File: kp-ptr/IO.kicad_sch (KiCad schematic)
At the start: 0 parts

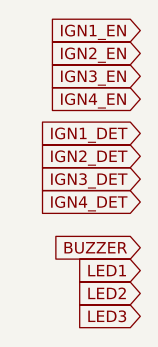
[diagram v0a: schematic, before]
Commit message: IGN & PSU added
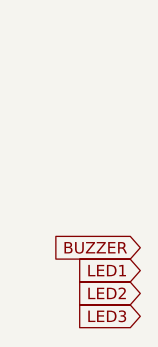
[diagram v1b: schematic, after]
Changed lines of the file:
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@@
 (kicad_sch (version 20211123) (generator eeschema)
   (paper "A4")
-  (global_label "IGN3_DET" (shape input) (at 36.83 41.91 180) (fields_autoplaced)
-    (effects (font (size 1.27 1.27)) (justify right))
-    (property "Intersheet References" "${INTERSHEET_REFS}" (id 0) (at 25.6479 41.8306 0)
-      (effects (font (size 1.27 1.27)) (justify right) hide)
-    )
-  )
-  (global_label "IGN1_EN" (shape input) (at 36.83 25.4 180) (fields_autoplaced)
-    (effects (font (size 1.27 1.27)) (justify right))
-    (property "Intersheet References" "${INTERSHEET_REFS}" (id 0) (at 26.555 25.3206 0)
-      (effects (font (size 1.27 1.27)) (justify right) hide)
-    )
-  )
   (global_label "LED3" (shape input) (at 36.83 57.15 180) (fields_autoplaced)
     (effects (font (size 1.27 1.27)) (justify right))
@@
     (effects (font (size 1.27 1.27)) (justify right))
     (property "Intersheet References" "${INTERSHEET_REFS}" (id 0) (at 29.7602 51.9906 0)
-      (effects (font (size 1.27 1.27)) (justify right) hide)
-    )
-  )
-  (global_label "IGN1_DET" (shape input) (at 36.83 36.83 180) (fields_autoplaced)
-    (effects (font (size 1.27 1.27)) (justify right))
-    (property "Intersheet References" "${INTERSHEET_REFS}" (id 0) (at 25.6479 36.7506 0)
-      (effects (font (size 1.27 1.27)) (justify right) hide)
-    )
-  )
-  (global_label "IGN3_EN" (shape input) (at 36.83 30.48 180) (fields_autoplaced)
-    (effects (font (size 1.27 1.27)) (justify right))
-    (property "Intersheet References" "${INTERSHEET_REFS}" (id 0) (at 26.555 30.4006 0)
-      (effects (font (size 1.27 1.27)) (justify right) hide)
-    )
-  )
-  (global_label "IGN2_DET" (shape input) (at 36.83 39.37 180) (fields_autoplaced)
-    (effects (font (size 1.27 1.27)) (justify right))
-    (property "Intersheet References" "${INTERSHEET_REFS}" (id 0) (at 25.6479 39.2906 0)
       (effects (font (size 1.27 1.27)) (justify right) hide)
     )
@@
       (effects (font (size 1.27 1.27)) (justify right) hide)
     )
-  )
-  (global_label "IGN2_EN" (shape input) (at 36.83 27.94 180) (fields_autoplaced)
-    (effects (font (size 1.27 1.27)) (justify right))
-    (property "Intersheet References" "${INTERSHEET_REFS}" (id 0) (at 26.555 27.8606 0)
-      (effects (font (size 1.27 1.27)) (justify right) hide)
-    )
-  )
-  (global_label "IGN4_DET" (shape input) (at 36.83 44.45 180) (fields_autoplaced)
-    (effects (font (size 1.27 1.27)) (justify right))
-    (property "Intersheet References" "${INTERSHEET_REFS}" (id 0) (at 25.6479 44.3706 0)
-      (effects (font (size 1.27 1.27)) (justify right) hide)
-    )
-  )
-  (global_label "IGN4_EN" (shape input) (at 36.83 33.02 180) (fields_autoplaced)
-    (effects (font (size 1.27 1.27)) (justify right))
-    (property "Intersheet References" "${INTERSHEET_REFS}" (id 0) (at 26.555 32.9406 0)
-      (effects (font (size 1.27 1.27)) (justify right) hide)
-    )

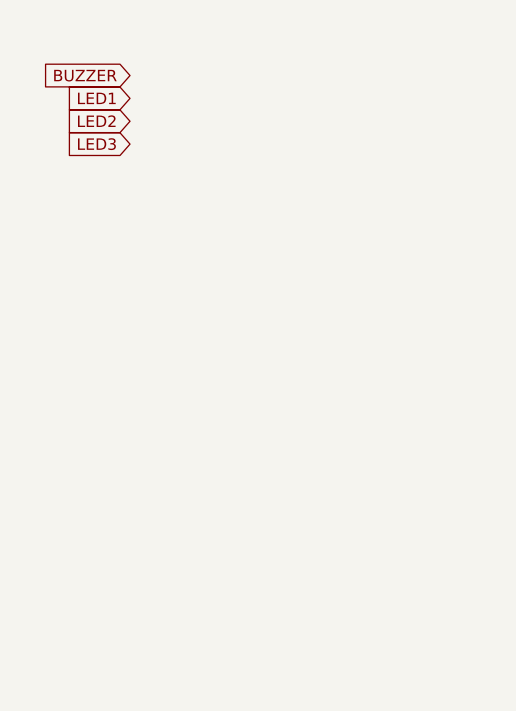
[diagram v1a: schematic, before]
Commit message: Magnetometr Buzzer 3xLED Signed-off-by: kretu <krecik@gmail.com>
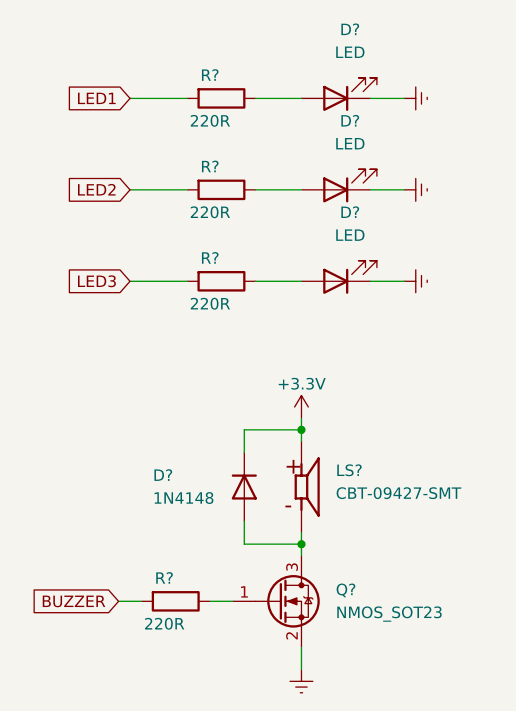
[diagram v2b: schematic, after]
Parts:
- added D? (x3): LED, symbol Device:LED
- added D?: 1N4148, Diode_THT:D_DO-35_SOD27_P7.62mm_Horizontal, symbol Diode:1N4148
- added LS?: CBT-09427-SMT, CUI_CBT-09427-SMT, symbol KP-PTR_lib:CBT-09427-SMT
- added Q?: NMOS_SOT23, Package_TO_SOT_SMD:SOT-23, symbol Transistor_FET:IRLML2060
- added R? (x4): 220R, symbol Device:R
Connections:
- net BUZZER: now also R?.2
- net LED1: now also R?.2
- net LED2: now also R?.2
- net LED3: now also R?.2
- new net: D?.2 (A), LS?.M, Q?.3 (D)
- new net: D?.2 (A), R?.1 (x3)
- new net: Q?.1 (G), R?.1
- new net +3V3: D?.1 (K), LS?.P
- new net Earth: D?.1 (K), D?.1 (K), D?.1 (K), Q?.2 (S)

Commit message: Footprints IN IMU9DOF OUT Signed-off-by: kretu <krecik@gmail.com>
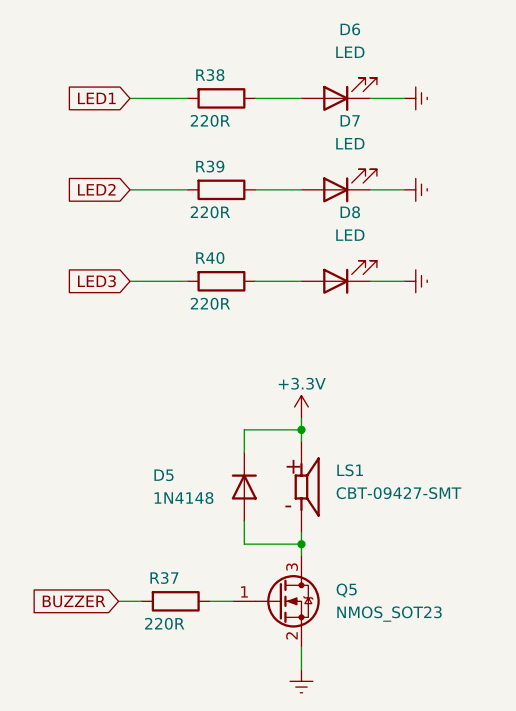
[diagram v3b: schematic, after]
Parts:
- D6, D7, D8: renamed from D?; footprint (none) -> LED_SMD:LED_0402_1005Metric_Pad0.77x0.64mm_HandSolder
- LS1: renamed from LS?; footprint CUI_CBT-09427-SMT -> KP-PTR_lib:BUZZER CBT-09
- R37, R38, R39: renamed from R?; footprint (none) -> Resistor_SMD:R_0402_1005Metric_Pad0.72x0.64mm_HandSolder
- R40: renamed from R?; footprint (none) -> Resistor_SMD:R_01005_0402Metric_Pad0.57x0.30mm_HandSolder
- gave numbers to parts that had none: 2
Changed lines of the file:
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@@
   (symbol (lib_id "KP-PTR_lib:CBT-09427-SMT") (at 55.88 95.25 0) (unit 1)
     (in_bom yes) (on_board yes) (fields_autoplaced)
-    (property "Reference" "LS?" (id 0) (at 59.69 93.4376 0)
+    (property "Reference" "LS1" (id 0) (at 59.69 93.4376 0)
       (effects (font (size 1.27 1.27)) (justify left))
     )
@@
       (effects (font (size 1.27 1.27)) (justify left))
     )
-    (property "Footprint" "CUI_CBT-09427-SMT" (id 2) (at 55.88 95.25 0)
+    (property "Footprint" "KP-PTR_lib:BUZZER CBT-09" (id 2) (at 55.88 95.25 0)
       (effects (font (size 1.27 1.27)) (justify left bottom) hide)
     )
@@
   (symbol (lib_id "power:Earth") (at 67.31 62.23 90) (unit 1)
     (in_bom yes) (on_board yes) (fields_autoplaced)
-    (property "Reference" "#PWR?" (id 0) (at 73.66 62.23 0)
+    (property "Reference" "#PWR0130" (id 0) (at 73.66 62.23 0)
       (effects (font (size 1.27 1.27)) hide)
     )
@@
   (symbol (lib_id "power:Earth") (at 67.31 72.39 90) (unit 1)
     (in_bom yes) (on_board yes) (fields_autoplaced)
-    (property "Reference" "#PWR?" (id 0) (at 73.66 72.39 0)
+    (property "Reference" "#PWR0131" (id 0) (at 73.66 72.39 0)
       (effects (font (size 1.27 1.27)) hide)
     )
@@
   (symbol (lib_id "Device:LED") (at 59.69 62.23 180) (unit 1)
     (in_bom yes) (on_board yes) (fields_autoplaced)
-    (property "Reference" "D?" (id 0) (at 61.2775 54.61 0))
+    (property "Reference" "D7" (id 0) (at 61.2775 54.61 0))
     (property "Value" "LED" (id 1) (at 61.2775 57.15 0))
-    (property "Footprint" "" (id 2) (at 59.69 62.23 0)
+    (property "Footprint" "LED_SMD:LED_0402_1005Metric_Pad0.77x0.64mm_HandSolder" (id 2) (at 59.69 62.23 0)
       (effects (font (size 1.27 1.27)) hide)
     )
@@
   (symbol (lib_id "Transistor_FET:IRLML2060") (at 53.34 107.95 0) (unit 1)
     (in_bom yes) (on_board yes) (fields_autoplaced)
-    (property "Reference" "Q?" (id 0) (at 59.69 106.6799 0)
+    (property "Reference" "Q5" (id 0) (at 59.69 106.6799 0)
       (effects (font (size 1.27 1.27)) (justify left))
     )
@@
   (symbol (lib_id "Device:R") (at 46.99 52.07 270) (unit 1)
     (in_bom yes) (on_board yes)
-    (property "Reference" "R?" (id 0) (at 45.72 49.53 90))
+    (property "Reference" "R38" (id 0) (at 45.72 49.53 90))
     (property "Value" "220R" (id 1) (at 45.72 54.61 90))
-    (property "Footprint" "" (id 2) (at 46.99 50.292 90)
+    (property "Footprint" "Resistor_SMD:R_0402_1005Metric_Pad0.72x0.64mm_HandSolder" (id 2) (at 46.99 50.292 90)
       (effects (font (size 1.27 1.27)) hide)
     )
@@
   (symbol (lib_id "Device:R") (at 46.99 62.23 270) (unit 1)
     (in_bom yes) (on_board yes)
-    (property "Reference" "R?" (id 0) (at 45.72 59.69 90))
+    (property "Reference" "R39" (id 0) (at 45.72 59.69 90))
     (property "Value" "220R" (id 1) (at 45.72 64.77 90))
-    (property "Footprint" "" (id 2) (at 46.99 60.452 90)
+    (property "Footprint" "Resistor_SMD:R_0402_1005Metric_Pad0.72x0.64mm_HandSolder" (id 2) (at 46.99 60.452 90)
       (effects (font (size 1.27 1.27)) hide)
     )
@@
   (symbol (lib_id "power:+3.3V") (at 55.88 87.63 0) (unit 1)
     (in_bom yes) (on_board yes)
-    (property "Reference" "#PWR?" (id 0) (at 55.88 91.44 0)
+    (property "Reference" "#PWR0127" (id 0) (at 55.88 91.44 0)
       (effects (font (size 1.27 1.27)) hide)
     )
@@
   (symbol (lib_id "Diode:1N4148") (at 49.53 95.25 270) (unit 1)
     (in_bom yes) (on_board yes)
-    (property "Reference" "D?" (id 0) (at 39.37 93.98 90)
+    (property "Reference" "D5" (id 0) (at 39.37 93.98 90)
       (effects (font (size 1.27 1.27)) (justify left))
     )
@@
   (symbol (lib_id "Device:R") (at 46.99 72.39 270) (unit 1)
     (in_bom yes) (on_board yes)
-    (property "Reference" "R?" (id 0) (at 45.72 69.85 90))
+    (property "Reference" "R40" (id 0) (at 45.72 69.85 90))
     (property "Value" "220R" (id 1) (at 45.72 74.93 90))
-    (property "Footprint" "" (id 2) (at 46.99 70.612 90)
+    (property "Footprint" "Resistor_SMD:R_01005_0402Metric_Pad0.57x0.30mm_HandSolder" (id 2) (at 46.99 70.612 90)
       (effects (font (size 1.27 1.27)) hide)
     )
@@
   (symbol (lib_id "power:Earth") (at 67.31 52.07 90) (unit 1)
     (in_bom yes) (on_board yes) (fields_autoplaced)
-    (property "Reference" "#PWR?" (id 0) (at 73.66 52.07 0)
+    (property "Reference" "#PWR0129" (id 0) (at 73.66 52.07 0)
       (effects (font (size 1.27 1.27)) hide)
     )
@@
   (symbol (lib_id "Device:R") (at 41.91 107.95 270) (unit 1)
     (in_bom yes) (on_board yes)
-    (property "Reference" "R?" (id 0) (at 40.64 105.41 90))
+    (property "Reference" "R37" (id 0) (at 40.64 105.41 90))
     (property "Value" "220R" (id 1) (at 40.64 110.49 90))
-    (property "Footprint" "" (id 2) (at 41.91 106.172 90)
+    (property "Footprint" "Resistor_SMD:R_0402_1005Metric_Pad0.72x0.64mm_HandSolder" (id 2) (at 41.91 106.172 90)
       (effects (font (size 1.27 1.27)) hide)
     )
@@
   (symbol (lib_id "power:Earth") (at 55.88 115.57 0) (unit 1)
     (in_bom yes) (on_board yes) (fields_autoplaced)
-    (property "Reference" "#PWR?" (id 0) (at 55.88 121.92 0)
+    (property "Reference" "#PWR0128" (id 0) (at 55.88 121.92 0)
       (effects (font (size 1.27 1.27)) hide)
     )
@@
   (symbol (lib_id "Device:LED") (at 59.69 52.07 180) (unit 1)
     (in_bom yes) (on_board yes) (fields_autoplaced)
-    (property "Reference" "D?" (id 0) (at 61.2775 44.45 0))
+    (property "Reference" "D6" (id 0) (at 61.2775 44.45 0))
     (property "Value" "LED" (id 1) (at 61.2775 46.99 0))
-    (property "Footprint" "" (id 2) (at 59.69 52.07 0)
+    (property "Footprint" "LED_SMD:LED_0402_1005Metric_Pad0.77x0.64mm_HandSolder" (id 2) (at 59.69 52.07 0)
       (effects (font (size 1.27 1.27)) hide)
     )
@@
   (symbol (lib_id "Device:LED") (at 59.69 72.39 180) (unit 1)
     (in_bom yes) (on_board yes) (fields_autoplaced)
-    (property "Reference" "D?" (id 0) (at 61.2775 64.77 0))
+    (property "Reference" "D8" (id 0) (at 61.2775 64.77 0))
     (property "Value" "LED" (id 1) (at 61.2775 67.31 0))
-    (property "Footprint" "" (id 2) (at 59.69 72.39 0)
-      (effects (font (size 1.27 1.27)) hide)
-    )
+    (property "Footprint" "LED_SMD:LED_0402_1005Metric_Pad0.77x0.64mm_HandSolder" (id 2) (at 59.69 72.39 0)
+      (effects (font (size 1.27 1.27)) hide)
+    )

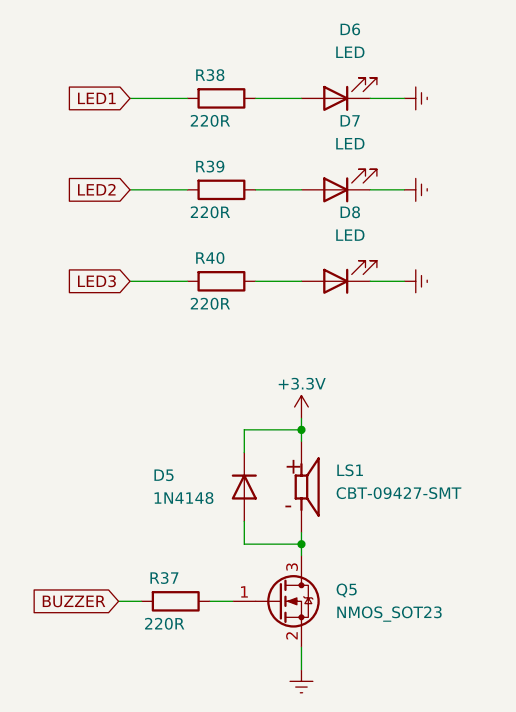
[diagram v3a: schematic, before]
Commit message: RF added, multiple small changes
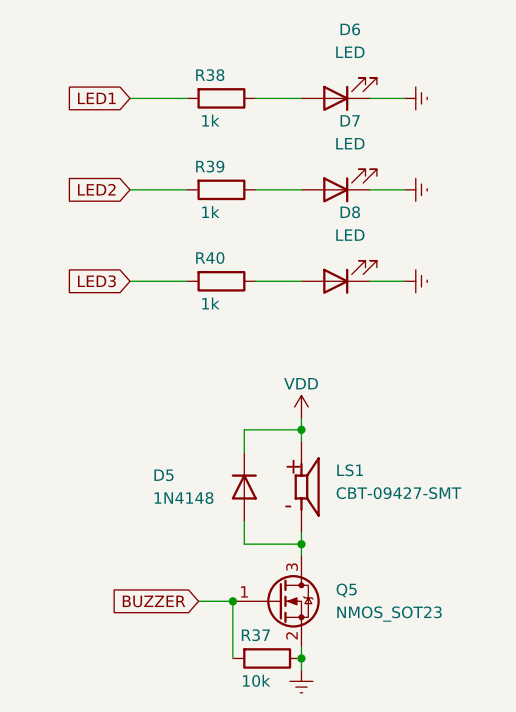
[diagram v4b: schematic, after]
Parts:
- R37: value 220R -> 10k
- R38, R39, R40: value 220R -> 1k
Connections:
- net BUZZER: now also Q5.1 (G)
- net Earth: now also R37.1
- net +3V3 renamed VDD
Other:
- moved on the sheet: R37
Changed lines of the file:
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@@
   (junction (at 55.88 101.6) (diameter 0) (color 0 0 0 0)
   )
+  (junction (at 55.88 114.3) (diameter 0) (color 0 0 0 0)
+  )
+  (junction (at 48.26 107.95) (diameter 0) (color 0 0 0 0)
+  )
   (junction (at 55.88 88.9) (diameter 0) (color 0 0 0 0)
   )
@@
     (stroke (width 0) (type default) (color 0 0 0 0))
   )
-  (wire (pts (xy 45.72 107.95) (xy 48.26 107.95))
-    (stroke (width 0) (type default) (color 0 0 0 0))
-  )
   (wire (pts (xy 49.53 99.06) (xy 49.53 101.6))
     (stroke (width 0) (type default) (color 0 0 0 0))
@@
     (stroke (width 0) (type default) (color 0 0 0 0))
   )
+  (wire (pts (xy 55.88 114.3) (xy 55.88 113.03))
+    (stroke (width 0) (type default) (color 0 0 0 0))
+  )
   (wire (pts (xy 36.83 52.07) (xy 43.18 52.07))
     (stroke (width 0) (type default) (color 0 0 0 0))
@@
     (stroke (width 0) (type default) (color 0 0 0 0))
   )
+  (wire (pts (xy 48.26 107.95) (xy 48.26 114.3))
+    (stroke (width 0) (type default) (color 0 0 0 0))
+  )
   (wire (pts (xy 67.31 62.23) (xy 63.5 62.23))
     (stroke (width 0) (type default) (color 0 0 0 0))
   )
-  (wire (pts (xy 35.56 107.95) (xy 38.1 107.95))
+  (wire (pts (xy 44.45 107.95) (xy 48.26 107.95))
     (stroke (width 0) (type default) (color 0 0 0 0))
   )
@@
     (stroke (width 0) (type default) (color 0 0 0 0))
   )
-  (wire (pts (xy 55.88 115.57) (xy 55.88 113.03))
+  (wire (pts (xy 55.88 115.57) (xy 55.88 114.3))
     (stroke (width 0) (type default) (color 0 0 0 0))
   )
@@
     )
   )
-  (global_label "BUZZER" (shape input) (at 35.56 107.95 180) (fields_autoplaced)
-    (effects (font (size 1.27 1.27)) (justify right))
-    (property "Intersheet References" "${INTERSHEET_REFS}" (id 0) (at 25.7083 107.8706 0)
+  (global_label "BUZZER" (shape input) (at 44.45 107.95 180) (fields_autoplaced)
+    (effects (font (size 1.27 1.27)) (justify right))
+    (property "Intersheet References" "${INTERSHEET_REFS}" (id 0) (at 34.5983 107.8706 0)
       (effects (font (size 1.27 1.27)) (justify right) hide)
     )
@@
     (pin "2")
   )
+  (symbol (lib_id "power:VDD") (at 55.88 87.63 0) (unit 1)
+    (in_bom yes) (on_board yes)
+    (property "Reference" "#PWR?" (id 0) (at 55.88 91.44 0)
+      (effects (font (size 1.27 1.27)) hide)
+    )
+    (property "Value" "VDD" (id 1) (at 55.88 83.82 0))
+    (property "Footprint" "" (id 2) (at 55.88 87.63 0)
+      (effects (font (size 1.27 1.27)) hide)
+    )
+    (property "Datasheet" "" (id 3) (at 55.88 87.63 0)
+      (effects (font (size 1.27 1.27)) hide)
+    )
+    (pin "1")
+  )
   (symbol (lib_id "Transistor_FET:IRLML2060") (at 53.34 107.95 0) (unit 1)
     (in_bom yes) (on_board yes) (fields_autoplaced)
@@
     (in_bom yes) (on_board yes)
     (property "Reference" "R38" (id 0) (at 45.72 49.53 90))
-    (property "Value" "220R" (id 1) (at 45.72 54.61 90))
+    (property "Value" "1k" (id 1) (at 45.72 54.61 90))
     (property "Footprint" "Resistor_SMD:R_0402_1005Metric_Pad0.72x0.64mm_HandSolder" (id 2) (at 46.99 50.292 90)
       (effects (font (size 1.27 1.27)) hide)
@@
     (in_bom yes) (on_board yes)
     (property "Reference" "R39" (id 0) (at 45.72 59.69 90))
-    (property "Value" "220R" (id 1) (at 45.72 64.77 90))
+    (property "Value" "1k" (id 1) (at 45.72 64.77 90))
     (property "Footprint" "Resistor_SMD:R_0402_1005Metric_Pad0.72x0.64mm_HandSolder" (id 2) (at 46.99 60.452 90)
       (effects (font (size 1.27 1.27)) hide)
@@
     (pin "2")
   )
-  (symbol (lib_id "power:+3.3V") (at 55.88 87.63 0) (unit 1)
-    (in_bom yes) (on_board yes)
-    (property "Reference" "#PWR0127" (id 0) (at 55.88 91.44 0)
-      (effects (font (size 1.27 1.27)) hide)
-    )
-    (property "Value" "+3.3V" (id 1) (at 55.88 83.82 0))
-    (property "Footprint" "" (id 2) (at 55.88 87.63 0)
-      (effects (font (size 1.27 1.27)) hide)
-    )
-    (property "Datasheet" "" (id 3) (at 55.88 87.63 0)
-      (effects (font (size 1.27 1.27)) hide)
-    )
-    (pin "1")
-  )
   (symbol (lib_id "Diode:1N4148") (at 49.53 95.25 270) (unit 1)
     (in_bom yes) (on_board yes)
@@
     (in_bom yes) (on_board yes)
     (property "Reference" "R40" (id 0) (at 45.72 69.85 90))
-    (property "Value" "220R" (id 1) (at 45.72 74.93 90))
+    (property "Value" "1k" (id 1) (at 45.72 74.93 90))
     (property "Footprint" "Resistor_SMD:R_01005_0402Metric_Pad0.57x0.30mm_HandSolder" (id 2) (at 46.99 70.612 90)
       (effects (font (size 1.27 1.27)) hide)
@@
     (pin "1")
   )
-  (symbol (lib_id "Device:R") (at 41.91 107.95 270) (unit 1)
-    (in_bom yes) (on_board yes)
-    (property "Reference" "R37" (id 0) (at 40.64 105.41 90))
-    (property "Value" "220R" (id 1) (at 40.64 110.49 90))
-    (property "Footprint" "Resistor_SMD:R_0402_1005Metric_Pad0.72x0.64mm_HandSolder" (id 2) (at 41.91 106.172 90)
-      (effects (font (size 1.27 1.27)) hide)
-    )
-    (property "Datasheet" "~" (id 3) (at 41.91 107.95 0)
-      (effects (font (size 1.27 1.27)) hide)
-    )
+  (symbol (lib_id "Device:R") (at 52.07 114.3 270) (unit 1)
+    (in_bom yes) (on_board yes)
+    (property "Reference" "R37" (id 0) (at 50.8 111.76 90))
+    (property "Value" "10k" (id 1) (at 50.8 116.84 90))
+    (property "Footprint" "Resistor_SMD:R_0402_1005Metric_Pad0.72x0.64mm_HandSolder" (id 2) (at 52.07 112.522 90)
+      (effects (font (size 1.27 1.27)) hide)
+    )
+    (property "Datasheet" "~" (id 3) (at 52.07 114.3 0)
+      (effects (font (size 1.27 1.27)) hide)
+    )

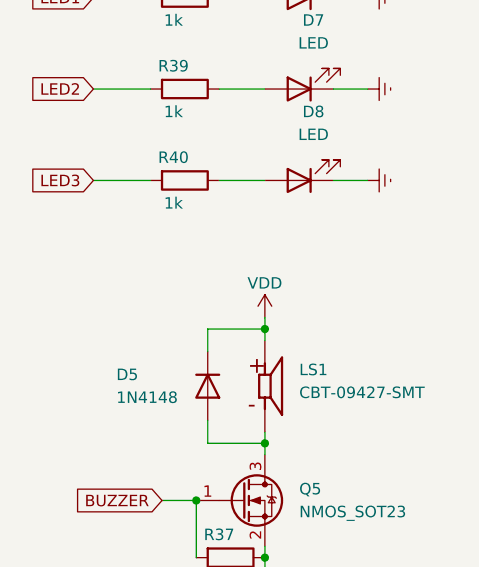
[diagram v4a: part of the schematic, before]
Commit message: Weryfikacja footprintow faza I Signed-off-by: kretu <krecik@gmail.com>
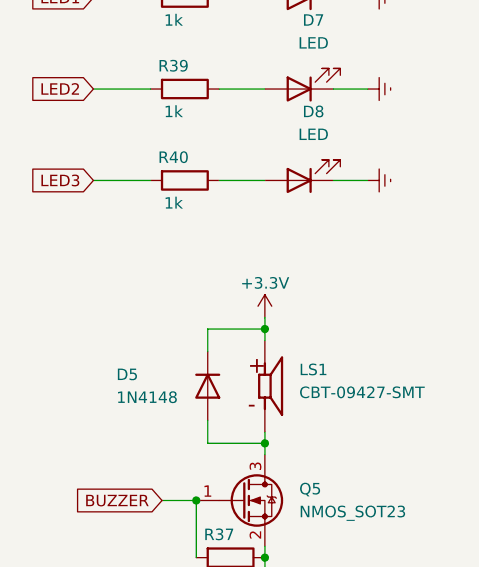
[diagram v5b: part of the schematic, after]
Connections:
- net VDD renamed +3V3
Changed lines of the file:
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@@
     (pin "2")
-  )
-  (symbol (lib_id "power:VDD") (at 55.88 87.63 0) (unit 1)
-    (in_bom yes) (on_board yes)
-    (property "Reference" "#PWR?" (id 0) (at 55.88 91.44 0)
-      (effects (font (size 1.27 1.27)) hide)
-    )
-    (property "Value" "VDD" (id 1) (at 55.88 83.82 0))
-    (property "Footprint" "" (id 2) (at 55.88 87.63 0)
-      (effects (font (size 1.27 1.27)) hide)
-    )
-    (property "Datasheet" "" (id 3) (at 55.88 87.63 0)
-      (effects (font (size 1.27 1.27)) hide)
-    )
-    (pin "1")
   )
   (symbol (lib_id "Transistor_FET:IRLML2060") (at 53.34 107.95 0) (unit 1)
@@
     (pin "3")
   )
+  (symbol (lib_id "power:+3.3V") (at 55.88 87.63 0) (unit 1)
+    (in_bom yes) (on_board yes)
+    (property "Reference" "#PWR0159" (id 0) (at 55.88 91.44 0)
+      (effects (font (size 1.27 1.27)) hide)
+    )
+    (property "Value" "+3.3V" (id 1) (at 55.88 83.82 0))
+    (property "Footprint" "" (id 2) (at 55.88 87.63 0)
+      (effects (font (size 1.27 1.27)) hide)
+    )
+    (property "Datasheet" "" (id 3) (at 55.88 87.63 0)
+      (effects (font (size 1.27 1.27)) hide)
+    )
+    (pin "1")
+  )
   (symbol (lib_id "Device:R") (at 46.99 52.07 270) (unit 1)
